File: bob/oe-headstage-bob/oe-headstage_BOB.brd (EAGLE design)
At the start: 160 x 100 mm, 13 parts, among them U1 SN65LVDS1DBVR, U2 SN65LVDS2DBVR, U3 SN65LVDS1DBVR, U4 SN65LVDS1DBVR

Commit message: Minor.
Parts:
- added C10: 0.1uF, rcl:C0603
- added C9: 1nF, rcl:C0603
- added S1, S2, S3: RHD2000-CABLE-DAQ-SIDE, RHD2000_eval_board:OMNETICS_PZN-12-AA
- added U$1: HDMI, open-ephys:HDMI_A
- added U5: SN65LVDS1DBVR, ti-extended:SOT95P280X145-5N
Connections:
- net +CS renamed +CS_A
- net -CS renamed -CS_A
- net CS renamed CS_A
- new net CS_B: U5.5
- new net N$10: S1.T4
- new net N$11: S1.B3
- new net N$12: S1.T3
- new net N$13: S1.B2
- new net N$14: S1.T2
- new net N$15: S1.B1
- new net N$16: S1.T1
- new net N$17: U$1.P$6
- new net N$18: U$1.P$7
- new net N$19: U$1.P$9
- new net N$20: U$1.P$10
- new net N$21: U$1.P$12
- new net N$5: C10.1, C9.1, U5.1
- new net N$6: S1.B5
- new net N$7: U$1.P$4
- new net N$8: S1.T5
- new net N$9: S1.B4
- new net VDRIVE: C1.1, C2.1, C5.1, C6.1, S1.B6, U$1.P$18, U3.1, U4.1
- net +SCLK: now also U5.4
- net -SCLK: now also U5.3
- net GND: now also C10.2, C9.2, S1.T6, S2.T6, S3.T6, U$1.P$11, U$1.P$2, U$1.P$5, U$1.P$8, U5.2
- net N$1: now also U$1.P$1; no longer C1.1, C2.1, U4.1
- net N$3: now also U$1.P$3; no longer C5.1, C6.1, U3.1
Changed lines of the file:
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@@
 <element name="C8" library="rcl" package="C0603" value="0.1uF" x="-30.48" y="49.53"/>
 <element name="R1" library="resistor" package="R0603" value="100" x="-43.18" y="38.1"/>
+<element name="S1" library="RHD2000_eval_board" package="OMNETICS_PZN-12-AA" value="RHD2000-CABLE-DAQ-SIDE" x="-53.34" y="5.08"/>
+<element name="U$1" library="open-ephys" package="HDMI_A" value="HDMI" x="-48.26" y="-5.08"/>
+<element name="U5" library="ti-extended" package="SOT95P280X145-5N" value="SN65LVDS1DBVR" x="-53.34" y="-16.51">
+<attribute name="PACKAGE" value="SOT-23-5" x="-53.34" y="-16.51" size="1.778" layer="27" display="off"/>
+<attribute name="OC_NEWARK" value="76C0715" x="-53.34" y="-16.51" size="1.778" layer="27" display="off"/>
+<attribute name="MPN" value="SN65LVDS1DBVR" x="-53.34" y="-16.51" size="1.778" layer="27" display="off"/>
+<attribute name="SUPPLIER" value="Texas Instruments" x="-53.34" y="-16.51" size="1.778" layer="27" display="off"/>
+<attribute name="OC_FARNELL" value="-" x="-53.34" y="-16.51" size="1.778" layer="27" display="off"/>
+<attribute name="DIGIKEY" value="296-6919-1-ND" x="-53.34" y="-16.51" size="1.778" layer="27" display="off"/>
+</element>
+<element name="C9" library="rcl" package="C0603" value="1nF" x="-55.88" y="-63.5"/>
+<element name="C10" library="rcl" package="C0603" value="0.1uF" x="-24.13" y="-46.99"/>
+<element name="S2" library="RHD2000_eval_board" package="OMNETICS_PZN-12-AA" value="RHD2000-CABLE-DAQ-SIDE" x="-60.96" y="-60.96"/>
+<element name="S3" library="RHD2000_eval_board" package="OMNETICS_PZN-12-AA" value="RHD2000-CABLE-DAQ-SIDE" x="-68.58" y="-60.96"/>
 </elements>
 <signals>
@@
 <signal name="-SCLK">
 <contactref element="U4" pad="3"/>
+<contactref element="U5" pad="3"/>
+<wire x1="-36.8554" y1="39.7002" x2="-54.6354" y2="-17.4498" width="0" layer="19" extent="1-1"/>
 </signal>
 <signal name="+SCLK">
 <contactref element="U4" pad="4"/>
-</signal>
-<signal name="N$1">
-<contactref element="U4" pad="1"/>
-<contactref element="C2" pad="1"/>
-<contactref element="C1" pad="1"/>
-<wire x1="-36.8554" y1="41.5798" x2="-36.41" y2="49.53" width="0" layer="19" extent="1-1"/>
-<wire x1="-50.38" y1="38.1" x2="-36.8554" y2="41.5798" width="0" layer="19" extent="1-1"/>
+<contactref element="U5" pad="4"/>
+<wire x1="-34.2646" y1="39.7002" x2="-52.0446" y2="-17.4498" width="0" layer="19" extent="1-1"/>
 </signal>
 <signal name="GND">
@@
 <contactref element="C7" pad="2"/>
 <contactref element="U2" pad="2"/>
-<wire x1="-16.93" y1="49.53" x2="-15.66" y2="54.61" width="0" layer="19" extent="1-1"/>
-<wire x1="-23.28" y1="49.53" x2="-16.93" y2="49.53" width="0" layer="19" extent="1-1"/>
-<wire x1="-29.63" y1="49.53" x2="-23.28" y2="49.53" width="0" layer="19" extent="1-1"/>
-<wire x1="-34.71" y1="49.53" x2="-29.63" y2="49.53" width="0" layer="19" extent="1-1"/>
+<contactref element="C10" pad="2"/>
+<contactref element="C9" pad="2"/>
+<contactref element="U5" pad="2"/>
+<contactref element="S2" pad="T6"/>
+<contactref element="S3" pad="T6"/>
+<contactref element="S1" pad="T6"/>
+<contactref element="U$1" pad="P$2"/>
+<contactref element="U$1" pad="P$5"/>
+<contactref element="U$1" pad="P$8"/>
+<contactref element="U$1" pad="P$11"/>
+<wire x1="-62.5475" y1="-63.119" x2="-70.1675" y2="-63.119" width="0" layer="19" extent="1-1"/>
+<wire x1="-55.03" y1="-63.5" x2="-62.5475" y2="-63.119" width="0" layer="19" extent="1-1"/>
+<wire x1="-23.28" y1="-46.99" x2="-55.03" y2="-63.5" width="0" layer="19" extent="1-1"/>
+<wire x1="-54.6354" y1="-16.51" x2="-23.28" y2="-46.99" width="0" layer="19" extent="1-1"/>
+<wire x1="-48.51" y1="-1.13" x2="-54.6354" y2="-16.51" width="0" layer="19" extent="1-1"/>
+<wire x1="-47.01" y1="-1.13" x2="-48.51" y2="-1.13" width="0" layer="19" extent="1-1"/>
+<wire x1="-45.51" y1="-1.13" x2="-47.01" y2="-1.13" width="0" layer="19" extent="1-1"/>
+<wire x1="-44.01" y1="-1.13" x2="-45.51" y2="-1.13" width="0" layer="19" extent="1-1"/>
+<wire x1="-54.9275" y1="2.921" x2="-48.51" y2="-1.13" width="0" layer="19" extent="1-1"/>
+<wire x1="-36.8554" y1="6.35" x2="-44.01" y2="-1.13" width="0" layer="19" extent="1-1"/>
+<wire x1="-36.8554" y1="17.78" x2="-36.8554" y2="6.35" width="0" layer="19" extent="1-1"/>
+<wire x1="-36.8554" y1="29.21" x2="-36.8554" y2="17.78" width="0" layer="19" extent="1-1"/>
+<wire x1="-36.8554" y1="40.64" x2="-36.8554" y2="29.21" width="0" layer="19" extent="1-1"/>
+<wire x1="-34.71" y1="49.53" x2="-36.8554" y2="40.64" width="0" layer="19" extent="1-1"/>
+<wire x1="-29.63" y1="49.53" x2="-34.71" y2="49.53" width="0" layer="19" extent="1-1"/>
 <wire x1="-39.79" y1="49.53" x2="-34.71" y2="49.53" width="0" layer="19" extent="1-1"/>
 <wire x1="-44.87" y1="49.53" x2="-39.79" y2="49.53" width="0" layer="19" extent="1-1"/>
-<wire x1="-36.8554" y1="40.64" x2="-34.71" y2="49.53" width="0" layer="19" extent="1-1"/>
-<wire x1="-36.8554" y1="29.21" x2="-36.8554" y2="40.64" width="0" layer="19" extent="1-1"/>
-<wire x1="-36.8554" y1="17.78" x2="-36.8554" y2="29.21" width="0" layer="19" extent="1-1"/>
-<wire x1="-36.8554" y1="6.35" x2="-36.8554" y2="17.78" width="0" layer="19" extent="1-1"/>
+<wire x1="-23.28" y1="49.53" x2="-29.63" y2="49.53" width="0" layer="19" extent="1-1"/>
+<wire x1="-16.93" y1="49.53" x2="-23.28" y2="49.53" width="0" layer="19" extent="1-1"/>
+<wire x1="-15.66" y1="54.61" x2="-16.93" y2="49.53" width="0" layer="19" extent="1-1"/>
 <wire x1="-48.68" y1="38.1" x2="-44.87" y2="49.53" width="0" layer="19" extent="1-1"/>
 </signal>
@@
 <wire x1="-18.63" y1="49.53" x2="-41.49" y2="49.53" width="0" layer="19" extent="1-1"/>
 </signal>
-<signal name="N$3">
-<contactref element="U3" pad="1"/>
-<contactref element="C6" pad="1"/>
-<contactref element="C5" pad="1"/>
-<wire x1="-46.57" y1="49.53" x2="-24.98" y2="49.53" width="0" layer="19" extent="1-1"/>
-<wire x1="-36.8554" y1="30.1498" x2="-46.57" y2="49.53" width="0" layer="19" extent="1-1"/>
-</signal>
 <signal name="MOSI">
 <contactref element="U1" pad="5"/>
@@
 <wire x1="-36.8554" y1="18.7198" x2="-31.33" y2="49.53" width="0" layer="19" extent="1-1"/>
 </signal>
-<signal name="CS">
-<contactref element="U3" pad="5"/>
-</signal>
-<signal name="-CS">
-<contactref element="U3" pad="3"/>
-</signal>
-<signal name="+CS">
-<contactref element="U3" pad="4"/>
-</signal>
 <signal name="MISO">
 <contactref element="U2" pad="5"/>
@@
 <wire x1="-44.03" y1="38.1" x2="-34.2646" y2="16.8402" width="0" layer="19" extent="1-1"/>
 </signal>
+<signal name="N$5">
+<contactref element="U5" pad="1"/>
+<contactref element="C10" pad="1"/>
+<contactref element="C9" pad="1"/>
+<wire x1="-24.98" y1="-46.99" x2="-56.73" y2="-63.5" width="0" layer="19" extent="1-1"/>
+<wire x1="-54.6354" y1="-15.5702" x2="-24.98" y2="-46.99" width="0" layer="19" extent="1-1"/>
+</signal>
+<signal name="CS_A">
+<contactref element="U3" pad="5"/>
+</signal>
+<signal name="-CS_A">
+<contactref element="U3" pad="3"/>
+</signal>
+<signal name="+CS_A">
+<contactref element="U3" pad="4"/>
+</signal>
+<signal name="VDRIVE">
+<contactref element="U4" pad="1"/>
+<contactref element="C2" pad="1"/>
+<contactref element="C1" pad="1"/>
+<contactref element="U3" pad="1"/>
+<contactref element="C6" pad="1"/>
+<contactref element="C5" pad="1"/>
+<contactref element="S1" pad="B6"/>
+<contactref element="U$1" pad="P$18"/>
+<wire x1="-52.01" y1="-1.13" x2="-54.9275" y2="4.064" width="0" layer="19" extent="1-1"/>
+<wire x1="-36.8554" y1="30.1498" x2="-54.9275" y2="4.064" width="0" layer="19" extent="1-1"/>
+<wire x1="-36.8554" y1="41.5798" x2="-36.8554" y2="30.1498" width="0" layer="19" extent="1-1"/>
+<wire x1="-36.41" y1="49.53" x2="-36.8554" y2="41.5798" width="0" layer="19" extent="1-1"/>
+<wire x1="-46.57" y1="49.53" x2="-36.41" y2="49.53" width="0" layer="19" extent="1-1"/>
+<wire x1="-24.98" y1="49.53" x2="-36.41" y2="49.53" width="0" layer="19" extent="1-1"/>
+<wire x1="-50.38" y1="38.1" x2="-46.57" y2="49.53" width="0" layer="19" extent="1-1"/>
+</signal>
+<signal name="CS_B">
+<contactref element="U5" pad="5"/>
+</signal>
+<signal name="N$6">
+<contactref element="S1" pad="B5"/>
+</signal>
+<signal name="N$8">
+<contactref element="S1" pad="T5"/>
+</signal>
+<signal name="N$9">
+<contactref element="S1" pad="B4"/>
+</signal>
+<signal name="N$10">
+<contactref element="S1" pad="T4"/>
+</signal>
+<signal name="N$11">
+<contactref element="S1" pad="B3"/>
+</signal>
+<signal name="N$12">
+<contactref element="S1" pad="T3"/>
+</signal>
+<signal name="N$13">
+<contactref element="S1" pad="B2"/>
+</signal>
+<signal name="N$14">
+<contactref element="S1" pad="T2"/>
+</signal>
+<signal name="N$15">
+<contactref element="S1" pad="B1"/>
+</signal>
+<signal name="N$16">
+<contactref element="S1" pad="T1"/>
+</signal>
+<signal name="N$1">
+<contactref element="U$1" pad="P$1"/>
+</signal>
+<signal name="N$3">
+<contactref element="U$1" pad="P$3"/>
+</signal>
+<signal name="N$7">
+<contactref element="U$1" pad="P$4"/>
+</signal>
+<signal name="N$17">
+<contactref element="U$1" pad="P$6"/>
+</signal>
+<signal name="N$18">
+<contactref element="U$1" pad="P$7"/>
+</signal>
+<signal name="N$19">
+<contactref element="U$1" pad="P$9"/>
+</signal>
+<signal name="N$20">
+<contactref element="U$1" pad="P$10"/>
+</signal>
+<signal name="N$21">
+<contactref element="U$1" pad="P$12"/>
+</signal>
 </signals>

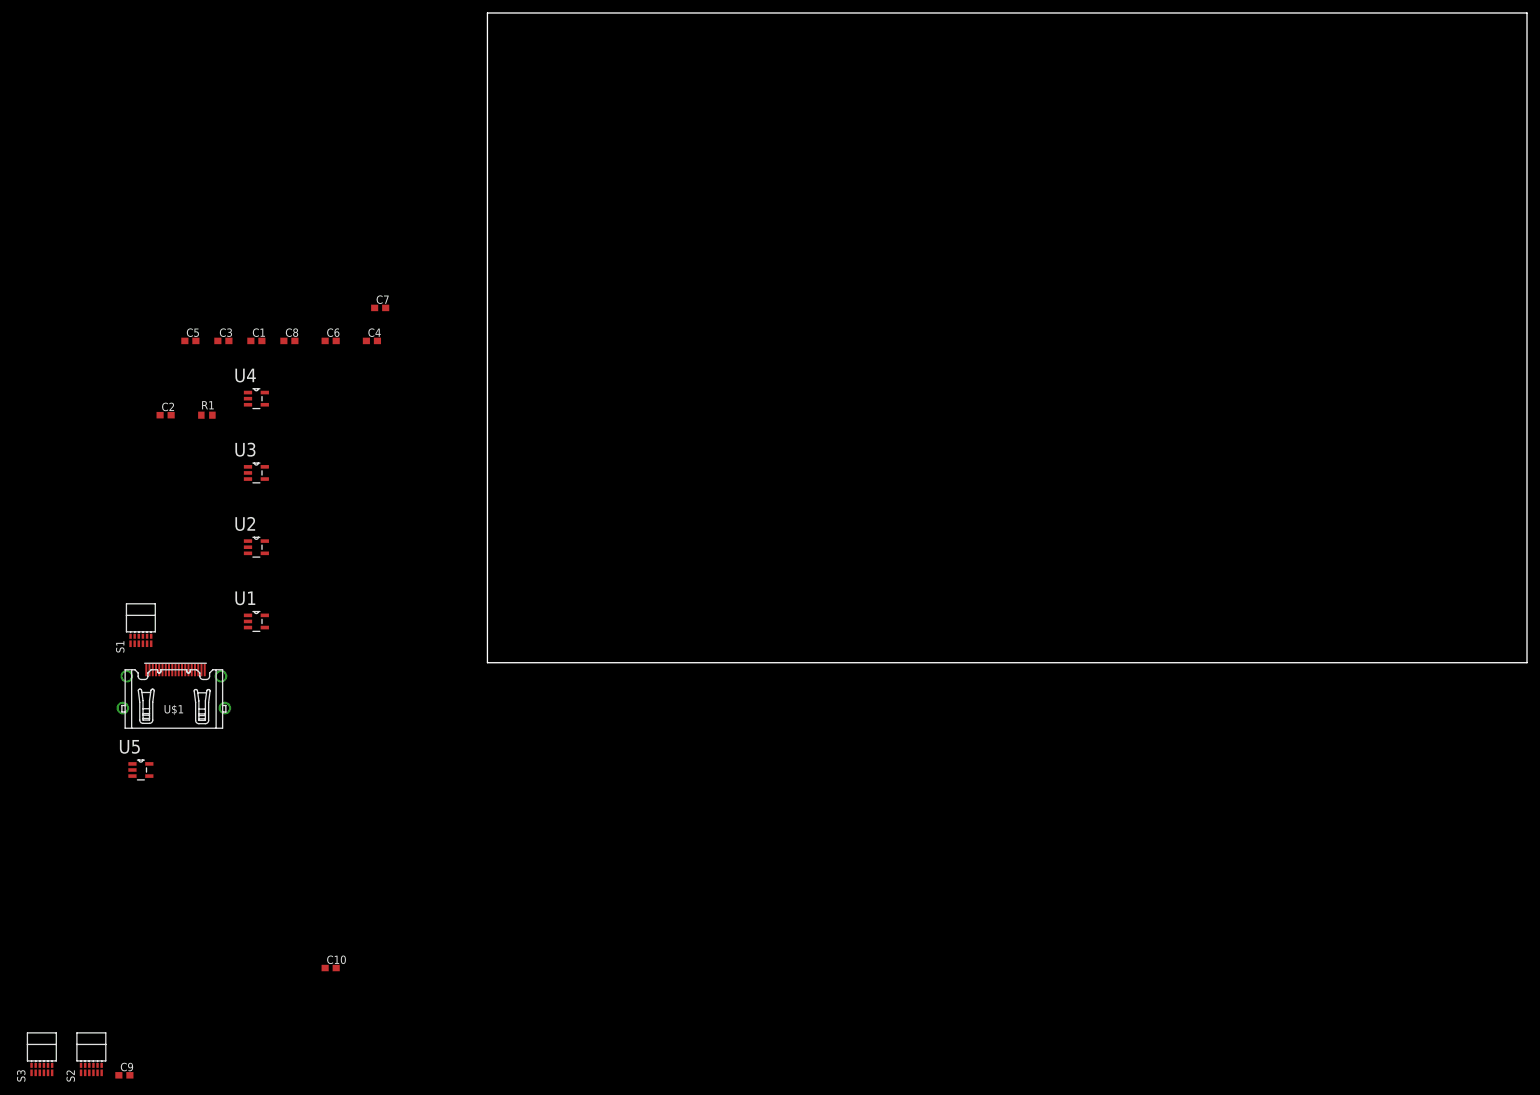
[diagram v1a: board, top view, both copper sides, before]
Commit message: Started differential routing on Intan BOB.
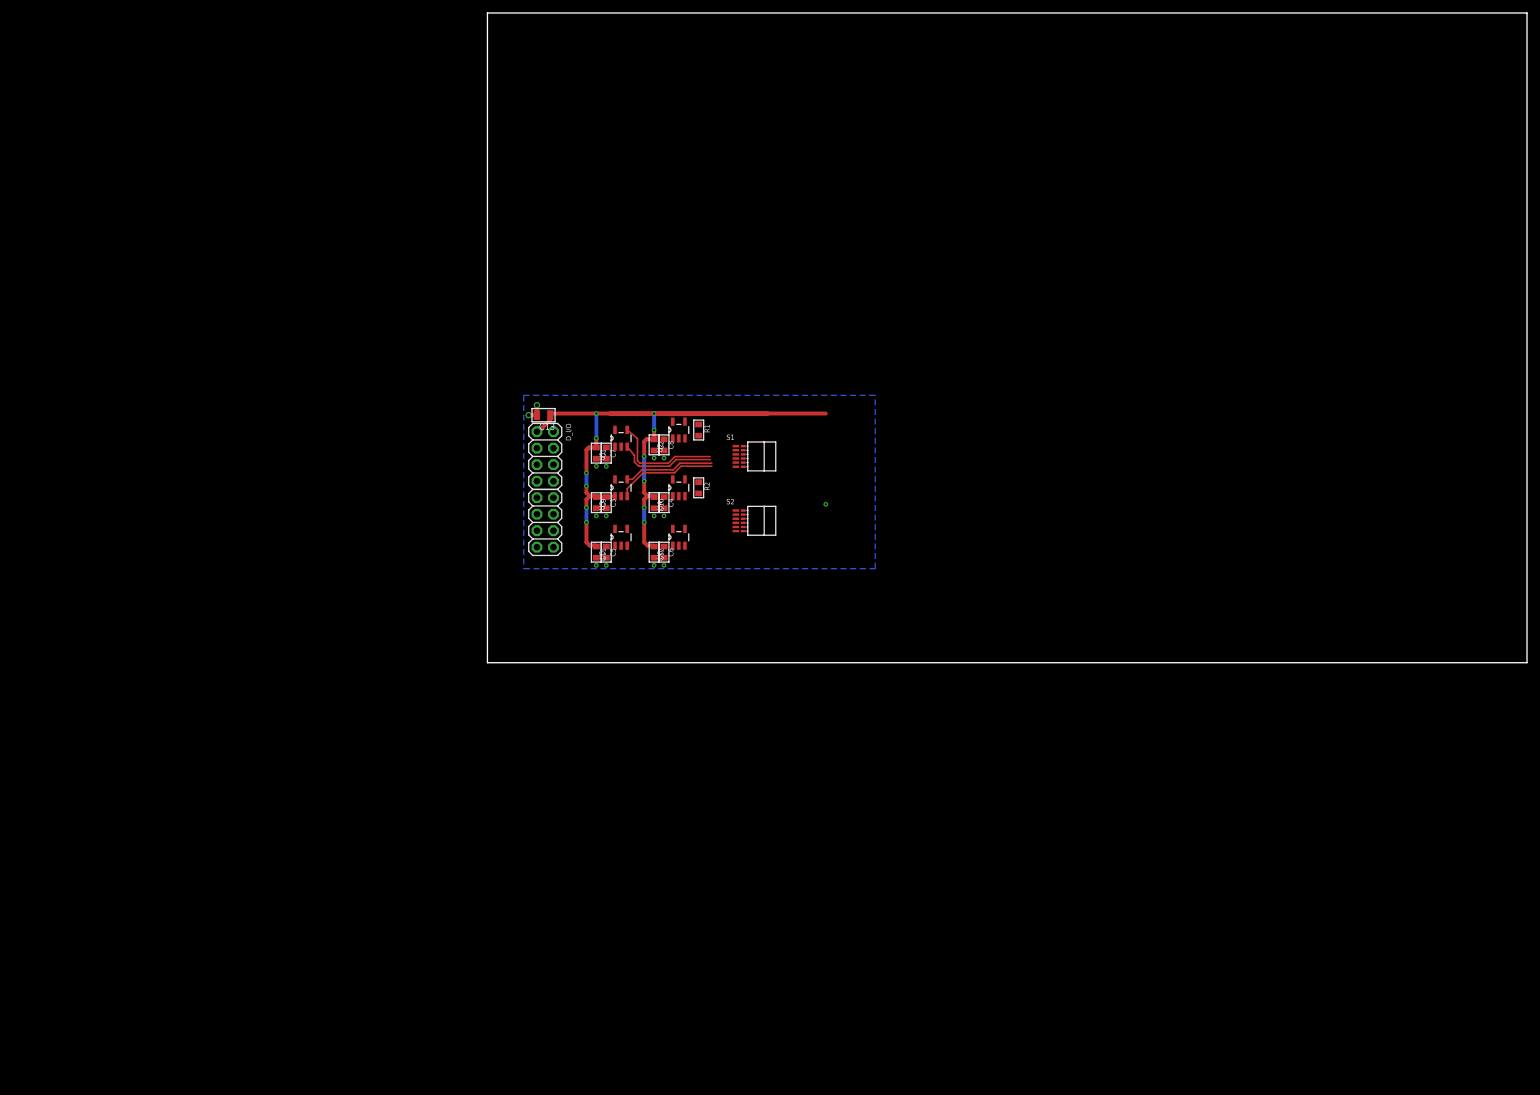
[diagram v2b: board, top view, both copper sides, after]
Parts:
- removed S3: RHD2000-CABLE-DAQ-SIDE, RHD2000_eval_board:OMNETICS_PZN-12-AA
- removed U$1: HDMI, open-ephys:HDMI_A
- added C11, C12: 1nF, puggleboard:0603
- added C13: 10uF, puggleboard:0805
- added D_I/O: PINHD-2X8VERT, adafruit:2X08
- added R2: 100, puggleboard:0603
- added U6: SN65LVDS1DBVR, ti-extended:SOT95P280X145-5N
- C1, C3, C5: value 1nF -> 0.1uF; device rcl:C0603 -> puggleboard:0603
- C10, C8: value 0.1uF -> 1nF; device rcl:C0603 -> puggleboard:0603
- C2, C4, C6, C7, C9: device rcl:C0603 -> puggleboard:0603
- R1: device resistor:R0603 -> puggleboard:0603
- U4: value SN65LVDS1DBVR -> SN65LVDS2DBVR
- moved S2 130.9 mm to (40.4, 21.8), turned to 270 degrees
- moved C9 114.2 mm to (16.8, 24.6), turned to 270 degrees
- moved S1 97.4 mm to (40.4, 31.8), turned to 270 degrees
- moved C10 87.2 mm to (25.7, 24.6), turned to 270 degrees
- moved U5 82.1 mm to (20.6, 19.3), turned to 90 degrees
- moved R1 75.7 mm to (32.5, 35.8), turned to 270 degrees
- moved C2 75.3 mm to (25.7, 33.5), turned to 270 degrees
- moved C5 71.8 mm to (18.3, 17.0), turned to 270 degrees
- moved U2 67.5 mm to (29.5, 35.8), turned to 90 degrees
- moved U4 66.5 mm to (29.5, 26.9), turned to 90 degrees
- moved C3 64.0 mm to (18.3, 24.6), turned to 270 degrees
- moved U1 62.8 mm to (20.6, 34.5), turned to 90 degrees
- moved C6 60.7 mm to (27.2, 17.0), turned to 270 degrees
- moved C8 59.8 mm to (27.2, 33.5), turned to 270 degrees
- moved U3 56.2 mm to (20.6, 26.9), turned to 90 degrees
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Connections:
- removed net +CS_A: U3.4
- removed net +MISO: R1.1, U2.4
- removed net +MOSI: U1.4
- removed net +SCLK: U4.4, U5.4
- removed net -CS_A: U3.3
- removed net -MISO: R1.2, U2.3
- removed net -MOSI: U1.3
- removed net -SCLK: U4.3, U5.3
- removed net CS_A: U3.5
- removed net CS_B: U5.5
- removed net MISO: U2.5
- removed net N$1: U$1.P$1
- removed net N$10: S1.T4
- removed net N$11: S1.B3
- removed net N$12: S1.T3
- removed net N$13: S1.B2
- removed net N$14: S1.T2
- removed net N$15: S1.B1
- removed net N$16: S1.T1
- removed net N$17: U$1.P$6
- removed net N$18: U$1.P$7
- removed net N$19: U$1.P$9
- removed net N$2: C3.1, C4.1, U1.1
- removed net N$20: U$1.P$10
- removed net N$21: U$1.P$12
- removed net N$3: U$1.P$3
- removed net N$4: C7.1, C8.1, U2.1
- removed net N$5: C10.1, C9.1, U5.1
- removed net N$6: S1.B5
- removed net N$7: U$1.P$4
- removed net N$8: S1.T5
- removed net N$9: S1.B4
- new net CS1: D_I/O.6, U3.5
- new net CS1_N: S1.T1, U3.3
- new net CS1_P: S1.B1, U3.4
- new net CS2: D_I/O.10, U5.5
- new net CS2_N: S2.T1, U5.3
- new net CS2_P: S2.B1, U5.4
- new net DIO_6: D_I/O.14
- new net DIO_7: D_I/O.16
- new net MISO1: D_I/O.4, U2.5
- new net MISO1_N: R1.2, S1.T4, U2.3
- new net MISO1_P: R1.1, S1.B4, U2.4
- new net MISO2: D_I/O.8, U4.5
- new net MISO2_N: R2.2, S2.T4, U4.3
- new net MISO2_P: R2.1, S2.B4, U4.4
- new net MOSI_N: S1.T3, S2.T3, U6.3
- new net MOSI_P: S1.B3, S2.B3, U6.4
- new net SCLK_N: S1.T2, S2.T2, U1.3
- new net SCLK_P: S1.B2, S2.B2, U1.4
- net GND: now also C11.2, C12.2, C13.2, D_I/O.11, D_I/O.13, D_I/O.15, D_I/O.3, D_I/O.5, D_I/O.7, D_I/O.9, U6.2; no longer S3.T6, U$1.P$11, U$1.P$2, U$1.P$5, U$1.P$8
- net MOSI: now also D_I/O.12, U6.5; no longer U1.5
- net SCLK: now also D_I/O.2, U1.5; no longer U4.5
- net VDRIVE: now also C10.1, C11.1, C12.1, C13.1, C3.1, C4.1, C7.1, C8.1, C9.1, D_I/O.1, S2.B6, U1.1, U2.1, U5.1, U6.1; no longer U$1.P$18
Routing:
- net VDRIVE: track 0.00 -> 64.5 mm, vias 0 -> 6
- net VDRIVE1: track 0.00 -> 57.2 mm, vias 0 -> 6
- net SCLK_P: track 0.00 -> 17.3 mm
- net CS1_N: track 0.00 -> 15.6 mm
- net SCLK_N: track 0.00 -> 15.1 mm
- net CS1_P: track 0.00 -> 14.1 mm
- net GND: track 0.00 -> 2.79 mm, vias 0 -> 15
- added copper zone on layer 16, net GND
